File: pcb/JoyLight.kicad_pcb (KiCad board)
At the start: 2 copper layers, 116.8 x 52.1 mm, 27 parts, among them J1 110990037, J2 110990037, J3 110990037, J4 110990037, J5 Conn_01x07_Male, J6 Conn_01x07_Male, SW1 SW_SPST, SW2 SW_SPST, SW3 SW_SPST, U1 SeeeduinoXIAO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

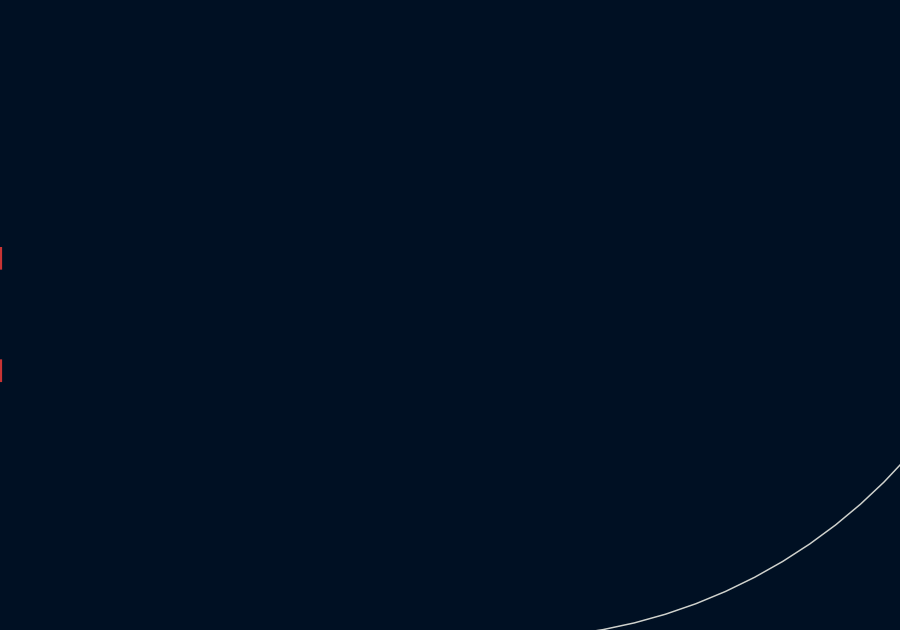
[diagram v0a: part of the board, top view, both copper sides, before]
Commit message: Getting the PCB ready for production
Updated the part numbers
Added silkscreen info
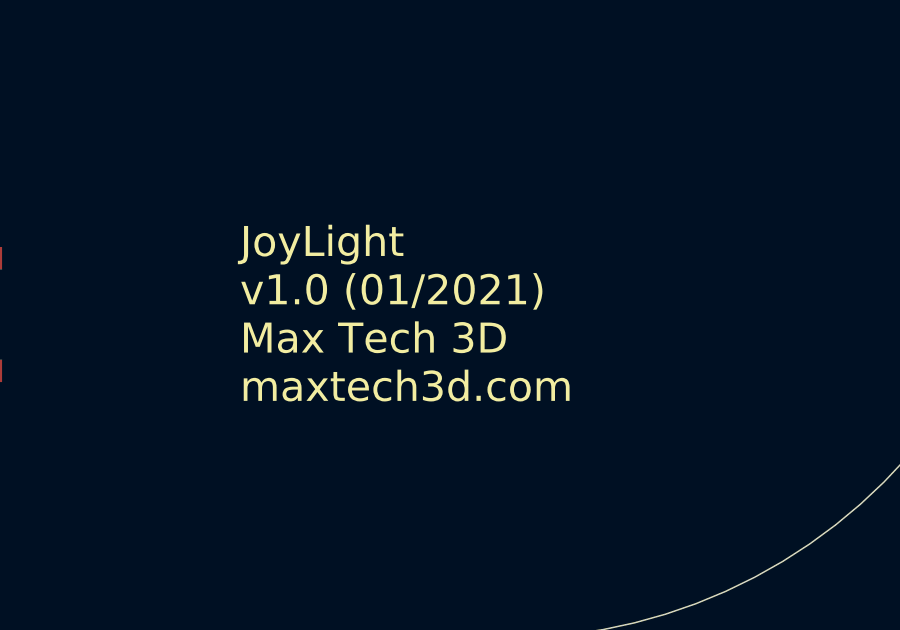
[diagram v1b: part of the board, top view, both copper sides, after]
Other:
- board text added: "JoyLight v1.0 (01/2021) Max Tech 3D maxtech3d.com"
